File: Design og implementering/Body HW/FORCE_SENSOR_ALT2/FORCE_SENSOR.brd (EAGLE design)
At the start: 68.6 x 47.1 mm, 15 parts, among them IC1 MCP6004P, J1 RJ11-6PTH, J2 RJ11-6PTH

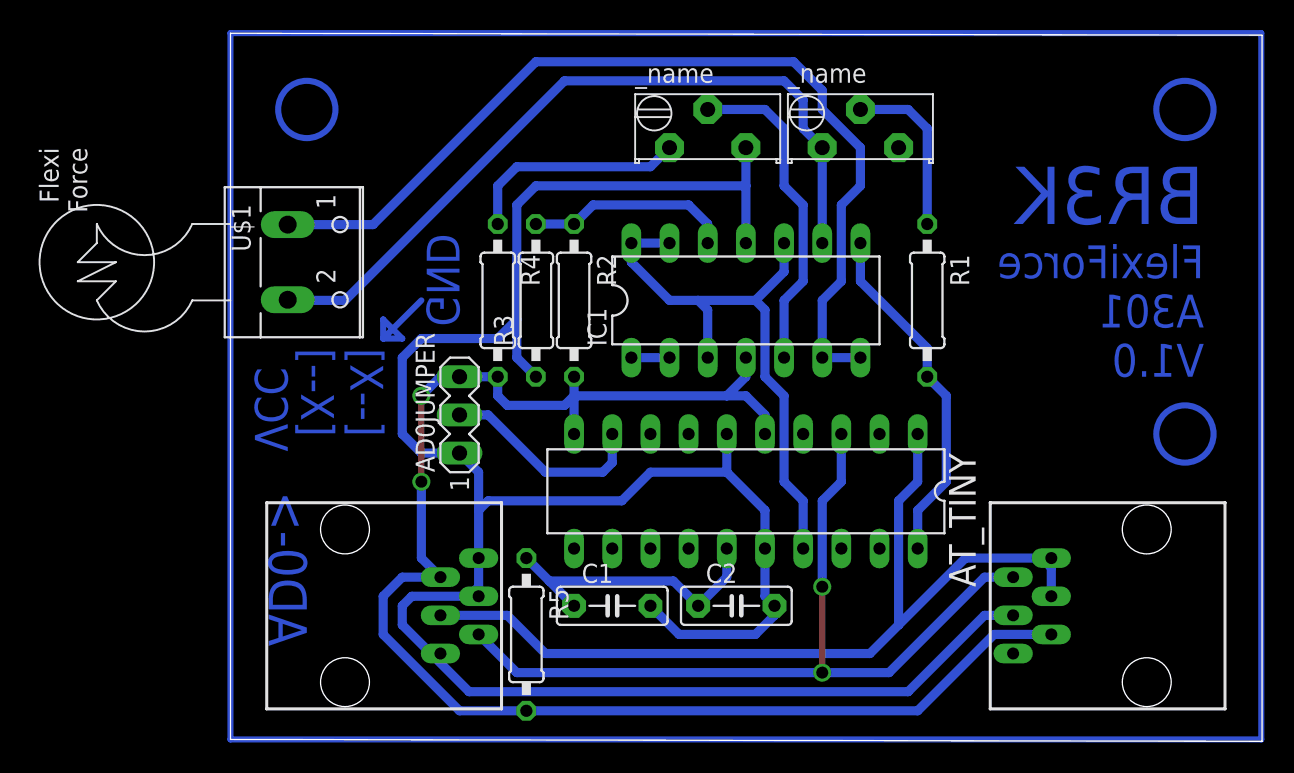
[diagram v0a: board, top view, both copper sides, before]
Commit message: Added improved Force sensor design -Felix
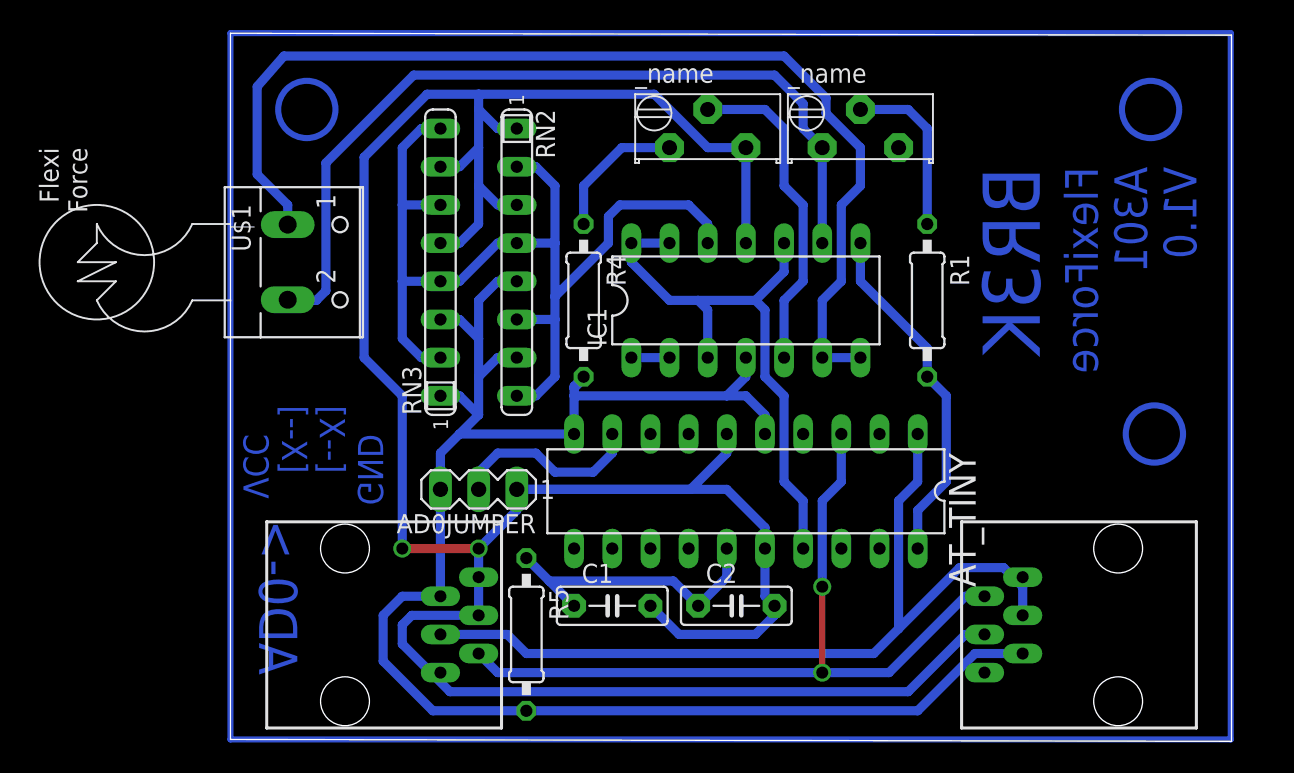
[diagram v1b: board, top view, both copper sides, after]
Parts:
- removed R2, R3: 1M Ohm, resistor:0207/10
- added RN2, RN3: (no value), resistor-sil:SIL8
- moved R4 5.71 mm to (26.0, 53.3)
- moved AD0JUMPER 5.11 mm to (19.1, 40.8), turned to 180 degrees
- moved J2 2.29 mm to (61.6, 26.7)
- moved J1 1.27 mm to (10.2, 36.8)
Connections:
- removed net N$2: IC1.12, R2.1, R3.2
- new net N$11: IC1.12, RN2.2, RN2.4, RN2.6, RN2.8, RN3.2, RN3.4, RN3.6, RN3.8
- net GND: now also RN2.1, RN2.3, RN3.5, RN3.7; no longer R3.1
- net VCC: now also RN2.5, RN2.7, RN3.1, RN3.3; no longer R2.2
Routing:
- net N$11: track 0.00 -> 69.5 mm
- net GND: track 154.2 -> 195.2 mm, vias 0 -> 2
- net VCC: track 102.0 -> 117.3 mm, vias 2 -> 0
- net N$2: track 13.8 -> 0.00 mm
- net SENS_SUPPLY: track 63.3 -> 71.8 mm
- net N$8: track 7.93 -> 0.00 mm
- net N$1: track 15.0 -> 9.31 mm
- net N$5: track 51.0 -> 56.2 mm
- net N$7: track 231.1 -> 227.1 mm
- net SCL: track 55.6 -> 52.7 mm
- net SDA: track 59.7 -> 57.5 mm
- net AD0_SELECT: track 13.9 -> 12.9 mm
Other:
- board size 68.6 x 47.1 mm -> 66.6 x 47.1 mm

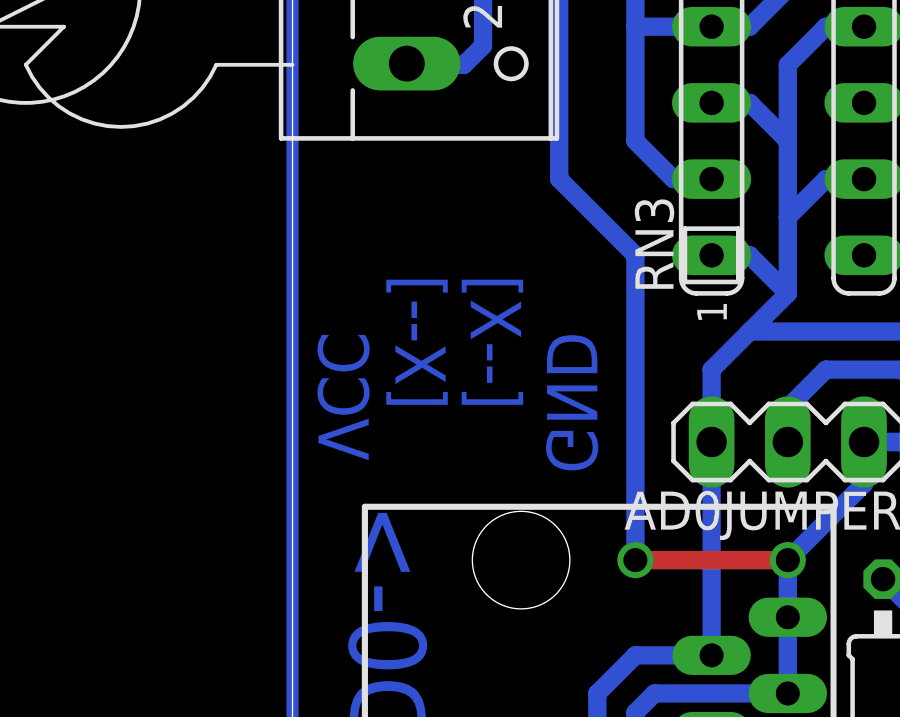
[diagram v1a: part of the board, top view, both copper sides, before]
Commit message: Finished the Force Sensor circuit and sent it and the mpu6050 board for production -Felix
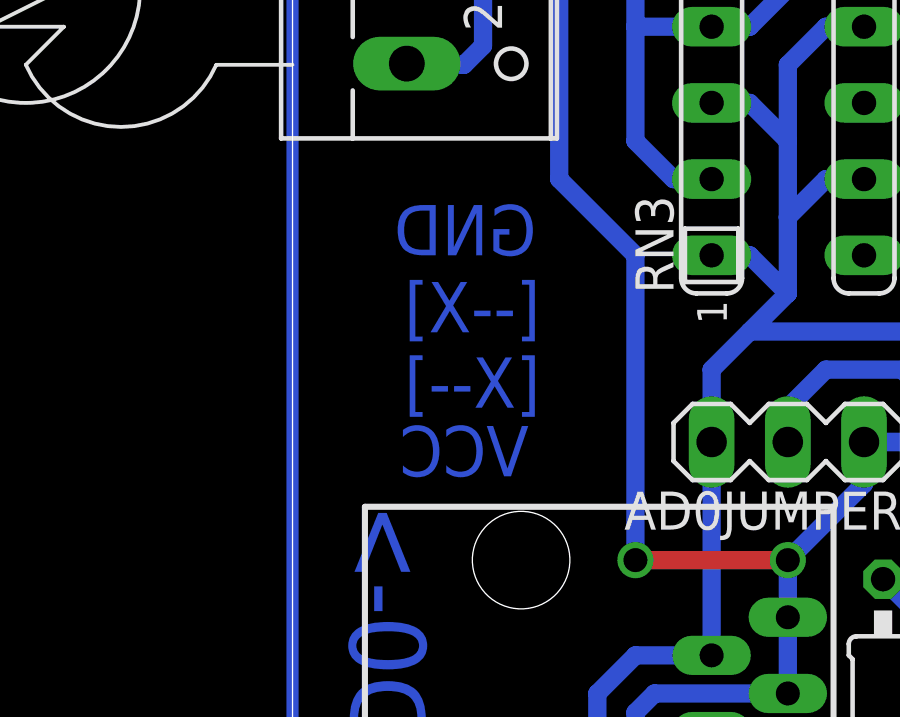
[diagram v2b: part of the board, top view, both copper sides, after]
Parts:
- RN2, RN3: value (none) -> 100kOhm
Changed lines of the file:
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@@
 <circle x="64.008" y="44.45" radius="1.905" width="0.4064" layer="16"/>
 <circle x="63.754" y="66.04" radius="1.905" width="0.4064" layer="16"/>
-<text x="10.16" y="46.355" size="1.6764" layer="16" font="vector" ratio="15" rot="MR270">[--X]
+<text x="10.795" y="41.91" size="1.6764" layer="16" font="vector" ratio="15" rot="MR0">[--X]
 [X--]</text>
-<text x="5.08" y="44.45" size="1.6764" layer="16" font="vector" ratio="15" rot="MR270">VCC</text>
-<text x="12.7" y="44.45" size="1.6764" layer="16" font="vector" ratio="15" rot="MR270">GND</text>
+<text x="10.414" y="39.624" size="1.6764" layer="16" font="vector" ratio="15" rot="MR0">VCC</text>
+<text x="10.668" y="46.99" size="1.6764" layer="16" font="vector" ratio="15" rot="MR0">GND</text>
 <text x="6.985" y="38.735" size="2.54" layer="16" font="vector" ratio="19" rot="MR270">AD0-&gt;</text>
 <text x="56.388" y="62.23" size="3.81" layer="16" font="vector" ratio="17" rot="SMR270">BR3K</text>
@@
 <attribute name="SPICEPREFIX" value="R" x="22.225" y="31.115" size="1.778" layer="27" rot="R270" display="off"/>
 </element>
-<element name="RN2" library="resistor-sil" package="SIL8" value="" x="21.59" y="55.88" rot="R270">
+<element name="RN2" library="resistor-sil" package="SIL8" value="100kOhm" x="21.59" y="55.88" rot="R270">
 <attribute name="OC_NEWARK" value="unknown" x="21.59" y="55.88" size="1.778" layer="27" rot="R270" display="off"/>
 <attribute name="MPN" value="" x="21.59" y="55.88" size="1.778" layer="27" rot="R270" display="off"/>
@@
 <attribute name="OC_FARNELL" value="unknown" x="21.59" y="55.88" size="1.778" layer="27" rot="R270" display="off"/>
 </element>
-<element name="RN3" library="resistor-sil" package="SIL8" value="" x="16.51" y="55.88" rot="R90">
+<element name="RN3" library="resistor-sil" package="SIL8" value="100kOhm" x="16.51" y="55.88" rot="R90">
 <attribute name="OC_NEWARK" value="unknown" x="16.51" y="55.88" size="1.778" layer="27" rot="R90" display="off"/>
 <attribute name="MPN" value="" x="16.51" y="55.88" size="1.778" layer="27" rot="R90" display="off"/>
